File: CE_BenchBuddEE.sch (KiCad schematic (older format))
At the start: 0 parts

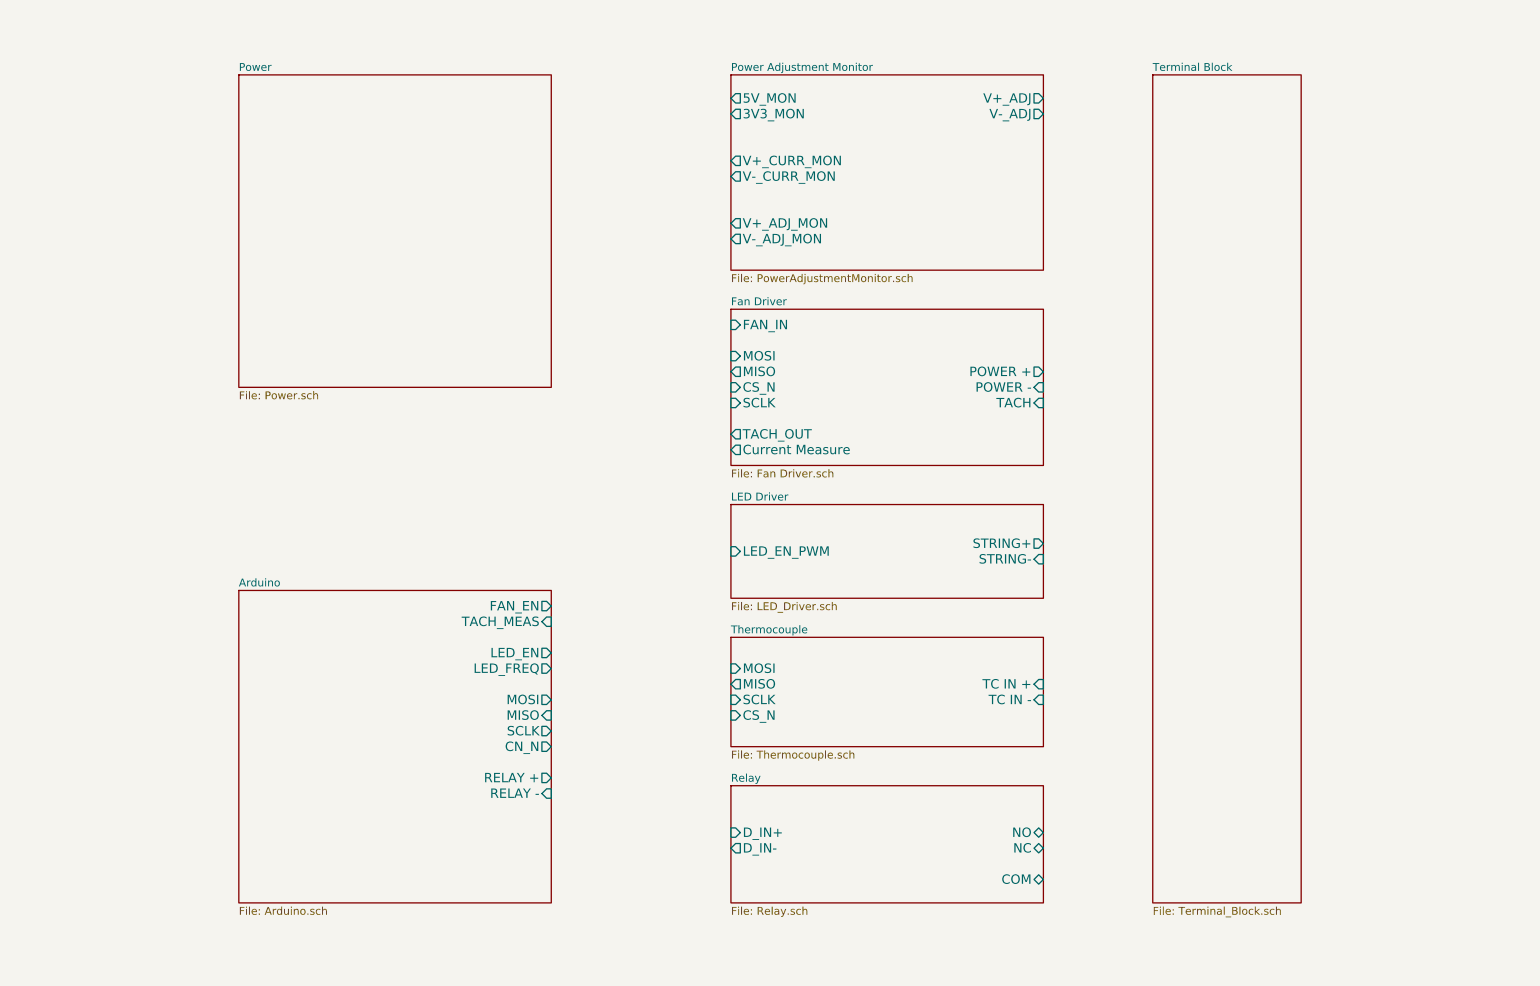
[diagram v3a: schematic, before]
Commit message: Completed Arduino Block Diagram and Fan Redesign
The commits as of this are now up to date with the videos released for
Contextual Electronics, Week 3.
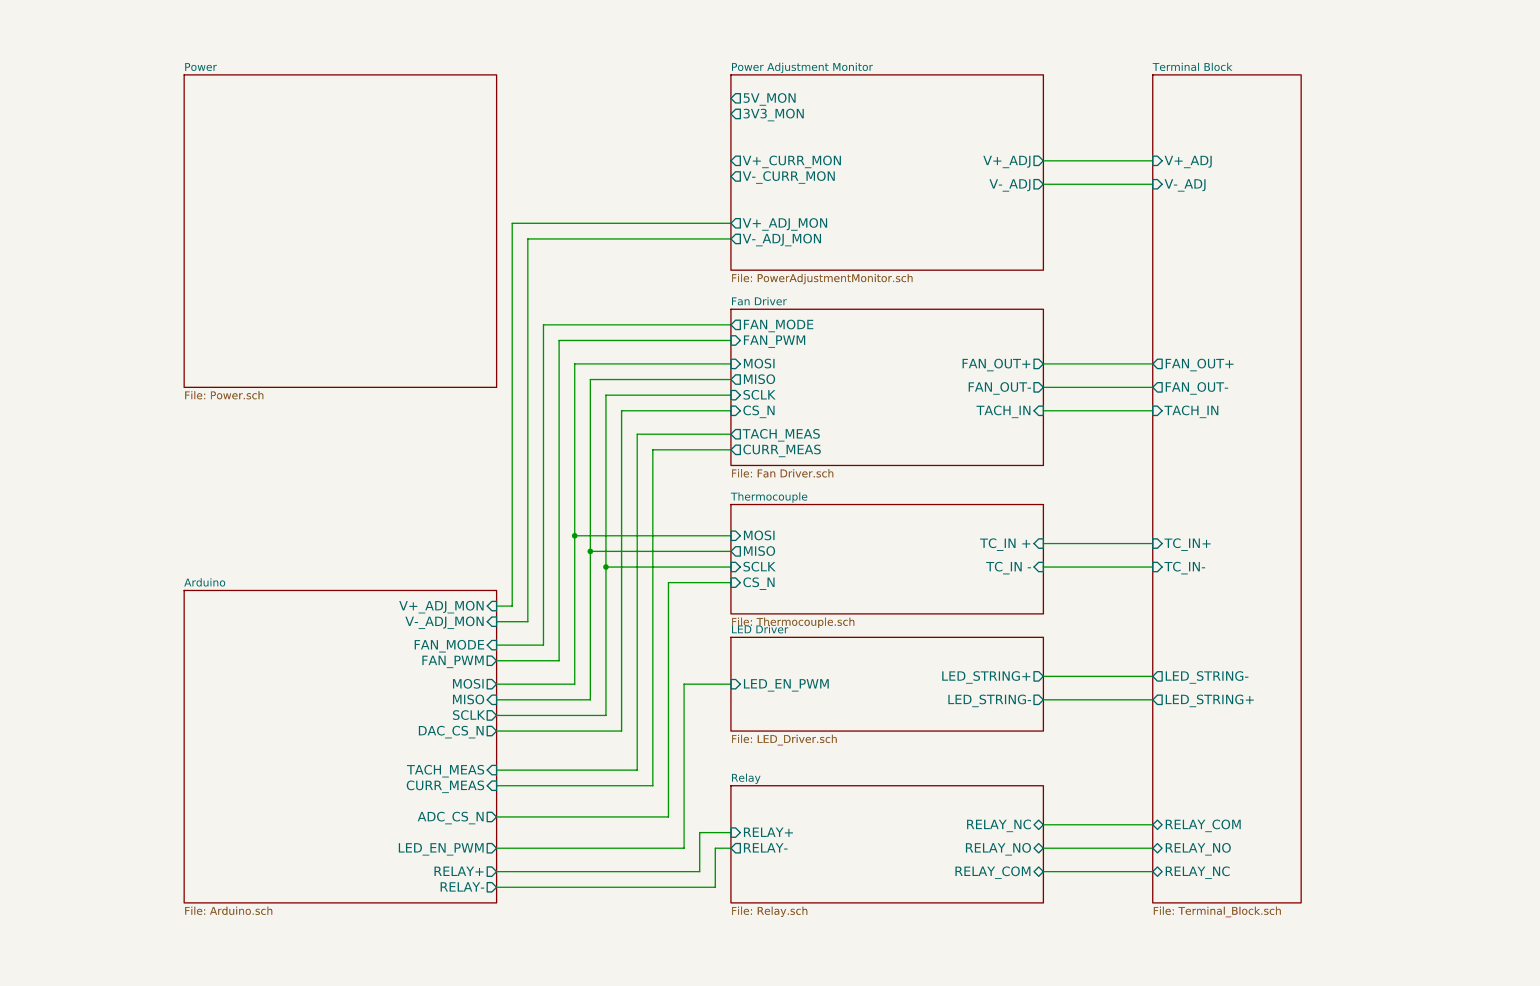
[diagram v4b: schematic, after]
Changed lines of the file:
@@
 $EndDescr
+$Sheet
+S 5400 4150 2000 700
+U 52EBF2F6
+F0 "Thermocouple" 50
+F1 "Thermocouple.sch" 50
+F2 "MOSI" I L 5400 4350 60
+F3 "MISO" O L 5400 4450 60
+F4 "SCLK" I L 5400 4550 60
+F5 "CS_N" I L 5400 4650 60
+F6 "TC_IN +" I R 7400 4400 60
+F7 "TC_IN -" I R 7400 4550 60
+$EndSheet
+$Sheet
+S 5400 5950 2000 750
+U 52EBF302
+F0 "Relay" 50
+F1 "Relay.sch" 50
+F2 "RELAY_NC" B R 7400 6200 60
+F3 "RELAY_NO" B R 7400 6350 60
+F4 "RELAY_COM" B R 7400 6500 60
+F5 "RELAY+" I L 5400 6250 60
+F6 "RELAY-" O L 5400 6350 60
+$EndSheet
+$Sheet
+S 1900 1400 2000 2000
+U 52EBF30F
+F0 "Power" 50
+F1 "Power.sch" 50
+$EndSheet
+$Sheet
+S 5400 5000 2000 600
+U 52EBF33E
+F0 "LED Driver" 50
+F1 "LED_Driver.sch" 50
+F2 "LED_EN_PWM" I L 5400 5300 60
+F3 "LED_STRING+" O R 7400 5250 60
+F4 "LED_STRING-" O R 7400 5400 60
+$EndSheet
+$Sheet
+S 5400 1400 2000 1250
+U 52F2E147
+F0 "Power Adjustment Monitor" 50
+F1 "PowerAdjustmentMonitor.sch" 50
+F2 "3V3_MON" O L 5400 1650 60
+F3 "5V_MON" O L 5400 1550 60
+F4 "V+_ADJ_MON" O L 5400 2350 60
+F5 "V-_ADJ_MON" O L 5400 2450 60
+F6 "V+_CURR_MON" O L 5400 1950 60
+F7 "V-_CURR_MON" O L 5400 2050 60
+F8 "V+_ADJ" O R 7400 1950 60
+F9 "V-_ADJ" O R 7400 2100 60
+$EndSheet
 $Sheet
 S 5400 2900 2000 1000
@@
 F0 "Fan Driver" 50
 F1 "Fan Driver.sch" 50
-F2 "POWER +" O R 7400 3300 60
-F3 "POWER -" I R 7400 3400 60
-F4 "TACH" I R 7400 3500 60
-F5 "TACH_OUT" O L 5400 3700 60
-F6 "FAN_IN" I L 5400 3000 60
-F7 "Current Measure" O L 5400 3800 60
-F8 "MOSI" I L 5400 3200 60
-F9 "MISO" O L 5400 3300 60
-F10 "CS_N" I L 5400 3400 60
-F11 "SCLK" I L 5400 3500 60
-$EndSheet
-$Sheet
-S 5400 5000 2000 700
-U 52EBF2F6
-F0 "Thermocouple" 50
-F1 "Thermocouple.sch" 50
-F2 "TC IN +" I R 7400 5300 60
-F3 "TC IN -" I R 7400 5400 60
-F4 "MOSI" I L 5400 5200 60
-F5 "MISO" O L 5400 5300 60
-F6 "SCLK" I L 5400 5400 60
-F7 "CS_N" I L 5400 5500 60
-$EndSheet
-$Sheet
-S 5400 5950 2000 750
-U 52EBF302
-F0 "Relay" 50
-F1 "Relay.sch" 50
-F2 "D_IN+" I L 5400 6250 60
-F3 "D_IN-" O L 5400 6350 60
-F4 "NC" B R 7400 6350 60
-F5 "NO" B R 7400 6250 60
-F6 "COM" B R 7400 6550 60
-$EndSheet
-$Sheet
-S 2250 4700 2000 2000
-U 52EBF29E
-F0 "Arduino" 50
-F1 "Arduino.sch" 50
-F2 "RELAY +" O R 4250 5900 60
-F3 "RELAY -" I R 4250 6000 60
-F4 "MOSI" O R 4250 5400 60
-F5 "MISO" I R 4250 5500 60
-F6 "SCLK" O R 4250 5600 60
-F7 "CN_N" O R 4250 5700 60
-F8 "LED_EN" O R 4250 5100 60
-F9 "LED_FREQ" O R 4250 5200 60
-F10 "FAN_EN" O R 4250 4800 60
-F11 "TACH_MEAS" I R 4250 4900 60
+F2 "MOSI" I L 5400 3250 60
+F3 "MISO" O L 5400 3350 60
+F4 "CS_N" I L 5400 3550 60
+F5 "SCLK" I L 5400 3450 60
+F6 "FAN_OUT+" O R 7400 3250 60
+F7 "TACH_IN" I R 7400 3550 60
+F8 "TACH_MEAS" O L 5400 3700 60
+F9 "CURR_MEAS" O L 5400 3800 60
+F10 "FAN_OUT-" O R 7400 3400 60
+F11 "FAN_PWM" I L 5400 3100 60
+F12 "FAN_MODE" O L 5400 3000 60
 $EndSheet
 $Sheet
@@
 F0 "Terminal Block" 50
 F1 "Terminal_Block.sch" 50
-$EndSheet
-$Sheet
-S 2250 1400 2000 2000
-U 52EBF30F
-F0 "Power" 50
-F1 "Power.sch" 50
-$EndSheet
-$Sheet
-S 5400 4150 2000 600
-U 52EBF33E
-F0 "LED Driver" 50
-F1 "LED_Driver.sch" 50
-F2 "STRING+" O R 7400 4400 60
-F3 "STRING-" I R 7400 4500 60
-F4 "LED_EN_PWM" I L 5400 4450 60
-$EndSheet
-$Sheet
-S 5400 1400 2000 1250
-U 52F2E147
-F0 "Power Adjustment Monitor" 50
-F1 "PowerAdjustmentMonitor.sch" 50
-F2 "V+_ADJ" O R 7400 1550 60
-F3 "V-_ADJ" O R 7400 1650 60
-F4 "3V3_MON" O L 5400 1650 60
-F5 "5V_MON" O L 5400 1550 60
-F6 "V+_ADJ_MON" O L 5400 2350 60
-F7 "V-_ADJ_MON" O L 5400 2450 60
-F8 "V+_CURR_MON" O L 5400 1950 60
-F9 "V-_CURR_MON" O L 5400 2050 60
-$EndSheet
+F2 "V+_ADJ" I L 8100 1950 60
+F3 "V-_ADJ" I L 8100 2100 60
+F4 "FAN_OUT+" O L 8100 3250 60
+F5 "FAN_OUT-" O L 8100 3400 60
+F6 "TACH_IN" I L 8100 3550 60
+F7 "LED_STRING+" O L 8100 5400 60
+F8 "LED_STRING-" O L 8100 5250 60
+F9 "TC_IN+" I L 8100 4400 60
+F10 "TC_IN-" I L 8100 4550 60
+F11 "RELAY_COM" B L 8100 6200 60
+F12 "RELAY_NO" B L 8100 6350 60
+F13 "RELAY_NC" B L 8100 6500 60
+$EndSheet
+$Sheet
+S 1900 4700 2000 2000
+U 52EBF29E
+F0 "Arduino" 50
+F1 "Arduino.sch" 50
+F2 "MOSI" O R 3900 5300 60
+F3 "MISO" I R 3900 5400 60
+F4 "SCLK" O R 3900 5500 60
+F5 "TACH_MEAS" I R 3900 5850 60
+F6 "LED_EN_PWM" O R 3900 6350 60
+F7 "CURR_MEAS" I R 3900 5950 60
+F8 "RELAY+" O R 3900 6500 60
+F9 "RELAY-" O R 3900 6600 60
+F10 "V+_ADJ_MON" I R 3900 4800 60
+F11 "V-_ADJ_MON" I R 3900 4900 60
+F12 "DAC_CS_N" O R 3900 5600 60
+F13 "ADC_CS_N" O R 3900 6150 60
+F14 "FAN_PWM" O R 3900 5150 60
+F15 "FAN_MODE" I R 3900 5050 60
+$EndSheet
+Wire Wire Line
+	8100 1950 7400 1950
+Wire Wire Line
+	8100 2100 7400 2100
+Wire Wire Line
+	7400 3250 8100 3250
+Wire Wire Line
+	7400 3400 8100 3400
+Wire Wire Line
+	8100 3550 7400 3550
+Wire Wire Line
+	7400 4400 8100 4400
+Wire Wire Line
+	8100 4550 7400 4550
+Wire Wire Line
+	7400 5250 8100 5250
+Wire Wire Line
+	7400 5400 8100 5400
+Wire Wire Line
+	7400 6200 8100 6200
+Wire Wire Line
+	7400 6350 8100 6350
+Wire Wire Line
+	7400 6500 8100 6500
+Wire Wire Line
+	3900 4800 4000 4800
+Wire Wire Line
+	4000 4800 4000 2350
+Wire Wire Line
+	4000 2350 5400 2350
+Wire Wire Line
+	5400 2450 4100 2450
+Wire Wire Line
+	4100 2450 4100 4900
+Wire Wire Line
+	4100 4900 3900 4900
+Wire Wire Line
+	5400 3700 4800 3700
+Wire Wire Line
+	5400 3800 4900 3800
+Wire Wire Line
+	3900 5850 4800 5850
+Wire Wire Line
+	4800 5850 4800 3700
+Wire Wire Line
+	4900 3800 4900 5950
+Wire Wire Line
+	4900 5950 3900 5950
+Wire Wire Line
+	3900 6150 5000 6150
+Wire Wire Line
+	5000 6150 5000 4650
+Wire Wire Line
+	5000 4650 5400 4650
+Wire Wire Line
+	3900 6350 5100 6350
+Wire Wire Line
+	5100 6350 5100 5300
+Wire Wire Line
+	5100 5300 5400 5300
+Wire Wire Line
+	3900 6500 5200 6500
+Wire Wire Line
+	5200 6500 5200 6250
+Wire Wire Line
+	5200 6250 5400 6250
+Wire Wire Line
+	5400 6350 5300 6350
+Wire Wire Line
+	5300 6350 5300 6600
+Wire Wire Line
+	5300 6600 3900 6600
+Wire Wire Line
+	4400 5300 3900 5300
+Wire Wire Line
+	4500 5400 3900 5400
+Wire Wire Line
+	4600 5500 3900 5500
+Wire Wire Line
+	5400 4350 4400 4350
+Connection ~ 4400 4350
+Wire Wire Line
+	5400 4450 4500 4450
+Connection ~ 4500 4450
+Wire Wire Line
+	5400 4550 4600 4550
+Connection ~ 4600 4550
+Wire Wire Line
+	3900 5600 4700 5600
+Wire Wire Line
+	5400 3100 4300 3100
+Wire Wire Line
+	4300 3100 4300 5150
+Wire Wire Line
+	4300 5150 3900 5150
+Wire Wire Line
+	3900 5050 4200 5050
+Wire Wire Line
+	4200 5050 4200 3000
+Wire Wire Line
+	4200 3000 5400 3000
+Wire Wire Line
+	4700 3550 5400 3550
+Wire Wire Line
+	4600 3450 5400 3450
+Wire Wire Line
+	4500 3350 5400 3350
+Wire Wire Line
+	4400 3250 5400 3250
+Wire Wire Line
+	4400 3250 4400 5300
+Wire Wire Line
+	4500 3350 4500 5400
+Wire Wire Line
+	4600 3450 4600 5500
+Wire Wire Line
+	4700 5600 4700 3550
 $EndSCHEMATC
